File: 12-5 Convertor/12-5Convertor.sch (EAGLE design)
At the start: 7 parts, among them U1 LM2678

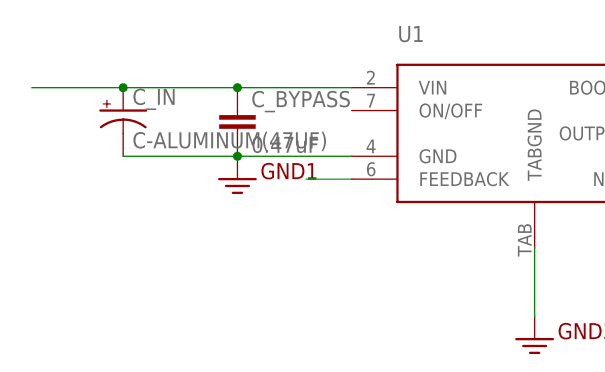
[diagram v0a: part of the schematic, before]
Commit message: adjust the dc-dc 12-5 convertor
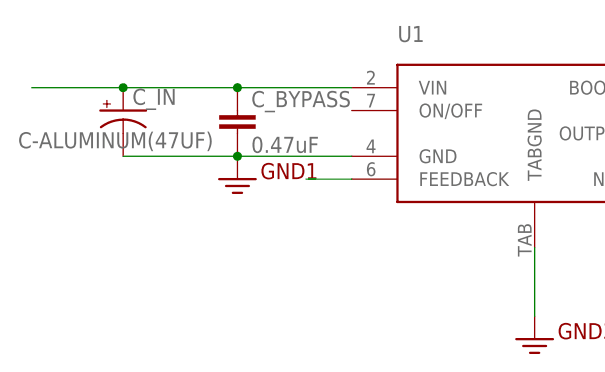
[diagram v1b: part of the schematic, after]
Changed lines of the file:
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@@
 <instance part="L1" gate="G$1" x="104.14" y="73.66" rot="R90"/>
 <instance part="C1" gate="G$1" x="129.54" y="68.58"/>
-<instance part="C_IN" gate="G$1" x="7.62" y="76.2"/>
+<instance part="C_IN" gate="G$1" x="7.62" y="76.2" smashed="yes">
+<attribute name="NAME" x="8.636" y="76.835" size="1.778" layer="95"/>
+<attribute name="VALUE" x="-4.064" y="72.009" size="1.778" layer="96"/>
+</instance>
 <instance part="C_BYPASS" gate="G$1" x="20.32" y="73.66"/>
 <instance part="C_BOOST" gate="G$1" x="83.82" y="78.74" smashed="yes" rot="R90">

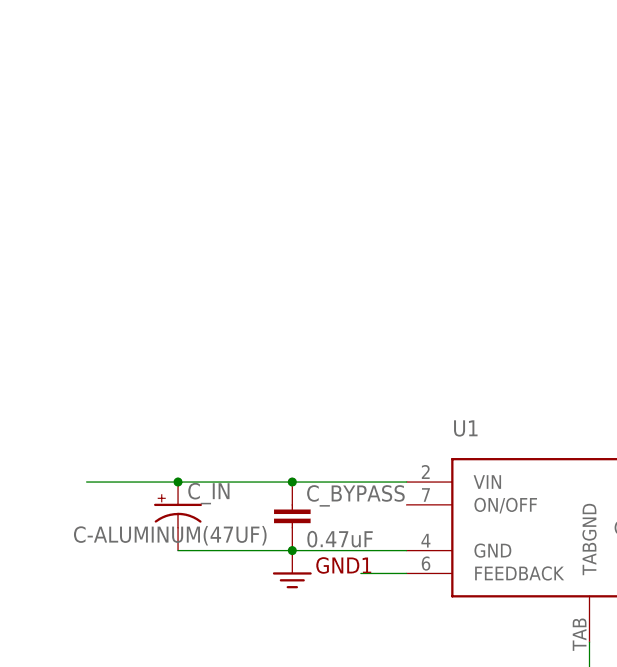
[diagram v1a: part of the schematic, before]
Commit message: Added Header Pins For testing
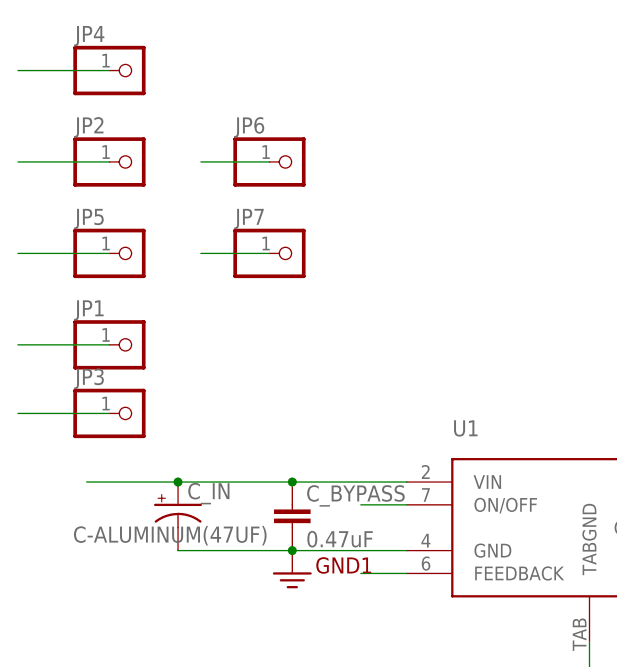
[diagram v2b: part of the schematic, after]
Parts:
- added JP1, JP2, JP3, JP4, JP5, JP6, JP7: (no value), pinhead:PINHD-1X1
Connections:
- removed net 5V: C1.+, L1.2, U1.FEEDBACK
- removed net VIN: C_BYPASS.1, C_IN.+, U1.VIN
- new net +12V: C_BYPASS.1, C_IN.+, JP1.1, JP3.1, U1.VIN
- new net +5V: C1.+, JP6.1, JP7.1, L1.2, U1.FEEDBACK
- new net ON/OFF: JP4.1, U1.ON/OFF
- net GND: now also JP2.1, JP5.1
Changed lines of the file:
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@@
 <part name="GND2" library="SparkFun-Aesthetics" deviceset="GND2" device=""/>
 <part name="GND3" library="SparkFun-Aesthetics" deviceset="GND2" device=""/>
+<part name="JP1" library="pinhead" deviceset="PINHD-1X1" device=""/>
+<part name="JP2" library="pinhead" deviceset="PINHD-1X1" device=""/>
+<part name="JP3" library="pinhead" deviceset="PINHD-1X1" device=""/>
+<part name="JP4" library="pinhead" deviceset="PINHD-1X1" device=""/>
+<part name="JP5" library="pinhead" deviceset="PINHD-1X1" device=""/>
+<part name="JP6" library="pinhead" deviceset="PINHD-1X1" device=""/>
+<part name="JP7" library="pinhead" deviceset="PINHD-1X1" device=""/>
 </parts>
 <sheets>
@@
 <instance part="GND2" gate="G$1" x="91.44" y="60.96"/>
 <instance part="GND3" gate="G$1" x="53.34" y="50.8"/>
+<instance part="JP1" gate="G$1" x="2.54" y="93.98"/>
+<instance part="JP2" gate="G$1" x="2.54" y="114.3"/>
+<instance part="JP3" gate="G$1" x="2.54" y="86.36"/>
+<instance part="JP4" gate="G$1" x="2.54" y="124.46"/>
+<instance part="JP5" gate="G$1" x="2.54" y="104.14"/>
+<instance part="JP6" gate="G$1" x="20.32" y="114.3"/>
+<instance part="JP7" gate="G$1" x="20.32" y="104.14"/>
 </instances>
 <busses>
 </busses>
 <nets>
-<net name="VIN" class="0">
-<segment>
-<pinref part="C_IN" gate="G$1" pin="+"/>
-<wire x1="7.62" y1="78.74" x2="-2.54" y2="78.74" width="0.1524" layer="91"/>
-<pinref part="C_BYPASS" gate="G$1" pin="1"/>
-<wire x1="7.62" y1="78.74" x2="20.32" y2="78.74" width="0.1524" layer="91"/>
-<junction x="7.62" y="78.74"/>
-<pinref part="U1" gate="G$1" pin="VIN"/>
-<wire x1="20.32" y1="78.74" x2="33.02" y2="78.74" width="0.1524" layer="91"/>
-<junction x="20.32" y="78.74"/>
-</segment>
-</net>
 <net name="N$2" class="0">
 <segment>
@@
 <pinref part="L1" gate="G$1" pin="1"/>
 <wire x1="88.9" y1="73.66" x2="96.52" y2="73.66" width="0.1524" layer="91"/>
-</segment>
-</net>
-<net name="5V" class="0">
-<segment>
-<pinref part="U1" gate="G$1" pin="FEEDBACK"/>
-<wire x1="33.02" y1="68.58" x2="27.94" y2="68.58" width="0.1524" layer="91"/>
-</segment>
-<segment>
-<pinref part="L1" gate="G$1" pin="2"/>
-<pinref part="C1" gate="G$1" pin="+"/>
-<wire x1="111.76" y1="73.66" x2="129.54" y2="73.66" width="0.1524" layer="91"/>
-<wire x1="129.54" y1="73.66" x2="129.54" y2="71.12" width="0.1524" layer="91"/>
-<wire x1="129.54" y1="73.66" x2="134.62" y2="73.66" width="0.1524" layer="91"/>
-<junction x="129.54" y="73.66"/>
 </segment>
 </net>
@@
 <wire x1="53.34" y1="53.34" x2="53.34" y2="60.96" width="0.1524" layer="91"/>
 </segment>
+<segment>
+<pinref part="JP2" gate="G$1" pin="1"/>
+<wire x1="0" y1="114.3" x2="-10.16" y2="114.3" width="0.1524" layer="91"/>
+</segment>
+<segment>
+<pinref part="JP5" gate="G$1" pin="1"/>
+<wire x1="0" y1="104.14" x2="-10.16" y2="104.14" width="0.1524" layer="91"/>
+</segment>
 </net>
+<net name="ON/OFF" class="0">
+<segment>
+<pinref part="JP4" gate="G$1" pin="1"/>
+<wire x1="0" y1="124.46" x2="-10.16" y2="124.46" width="0.1524" layer="91"/>
+</segment>
+<segment>
+<pinref part="U1" gate="G$1" pin="ON/OFF"/>
+<wire x1="33.02" y1="76.2" x2="27.94" y2="76.2" width="0.1524" layer="91"/>
+</segment>
+</net>
+<net name="+12V" class="0">
+<segment>
+<pinref part="C_IN" gate="G$1" pin="+"/>
+<wire x1="7.62" y1="78.74" x2="-2.54" y2="78.74" width="0.1524" layer="91"/>
+<pinref part="C_BYPASS" gate="G$1" pin="1"/>
+<wire x1="7.62" y1="78.74" x2="20.32" y2="78.74" width="0.1524" layer="91"/>
+<junction x="7.62" y="78.74"/>
+<pinref part="U1" gate="G$1" pin="VIN"/>
+<wire x1="20.32" y1="78.74" x2="33.02" y2="78.74" width="0.1524" layer="91"/>
+<junction x="20.32" y="78.74"/>
+</segment>
+<segment>
+<pinref part="JP3" gate="G$1" pin="1"/>
+<wire x1="0" y1="86.36" x2="-10.16" y2="86.36" width="0.1524" layer="91"/>
+</segment>
+<segment>
+<pinref part="JP1" gate="G$1" pin="1"/>
+<wire x1="0" y1="93.98" x2="-10.16" y2="93.98" width="0.1524" layer="91"/>
+</segment>
+</net>
+<net name="+5V" class="0">
+<segment>
+<pinref part="L1" gate="G$1" pin="2"/>
+<pinref part="C1" gate="G$1" pin="+"/>
+<wire x1="111.76" y1="73.66" x2="129.54" y2="73.66" width="0.1524" layer="91"/>
+<wire x1="129.54" y1="73.66" x2="129.54" y2="71.12" width="0.1524" layer="91"/>
+<wire x1="129.54" y1="73.66" x2="134.62" y2="73.66" width="0.1524" layer="91"/>
+<junction x="129.54" y="73.66"/>
+</segment>
+<segment>
+<pinref part="U1" gate="G$1" pin="FEEDBACK"/>
+<wire x1="33.02" y1="68.58" x2="27.94" y2="68.58" width="0.1524" layer="91"/>
+</segment>
+<segment>
+<pinref part="JP6" gate="G$1" pin="1"/>
+<wire x1="17.78" y1="114.3" x2="10.16" y2="114.3" width="0.1524" layer="91"/>
+</segment>
+<segment>
+<pinref part="JP7" gate="G$1" pin="1"/>
+<wire x1="17.78" y1="104.14" x2="10.16" y2="104.14" width="0.1524" layer="91"/>
+</segment>
+</net>
